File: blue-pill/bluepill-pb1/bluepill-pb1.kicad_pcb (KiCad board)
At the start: 2 copper layers, 102.9 x 68.6 mm, 31 parts, among them J1 pc850vs_11_pin, J2 Conn_01x04, J3 Conn_01x04, J4 Conn_01x04, J5 Conn_01x09, J6 Conn_01x06, J7 Conn_01x02, Q1 Q_NPN_CBE, SW1 Switch_SW_SPST, SW2 Switch_SW_SPST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

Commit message: Added samples
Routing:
- net (no net): vias 107 -> 111
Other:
- board size 102.9 x 68.6 mm -> 102.9 x 88.8 mm
- board text added: "SHARP PC-G850VS Gadget V2.1"
- board text removed: "SHARP PC-G850VS Gadget V2.0"

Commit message: Fix to issue #2
The SD card would sometimes not initialise. A possible fix to this is in this
commit.
By putting a finger on various terminals I found that the CS pin of the SD card adapter
could stop initialisation of the card if it was held high. Holding it low with a high-ish
resistance allowed the SD card to initialise every time. With the theory that the CS line
was activating before or during the SD card initialisation and messing it up, holding it low with a resistor
would deselect it unless the blue pill drove the GPIO high when it wanted ot send a command
or data.
As a test, I have added an explicit GPIO output data direction setup and drive the GPIo to 0 as early
as possible. This does seem to have solved the problem I saw, which hopefully is the problem
seen everywhere.
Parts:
- R1, R16, R17, R2, R3: value R_Small -> 4k7
- R10, R11, R12, R13, R4, R5, R6, R7, R8, R9: value R_Small -> 1k
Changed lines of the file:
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@@
-(kicad_pcb (version 20171130) (host pcbnew 5.1.6-c6e7f7d~86~ubuntu16.04.1)
+(kicad_pcb (version 20171130) (host pcbnew 5.1.5+dfsg1-2build2)
   (general
     (thickness 1.6)
@@
     (add_net "Net-(A1-Pad5)")
     (add_net "Net-(A1-Pad6)")
+    (add_net "Net-(J1-Pad1)")
     (add_net "Net-(J1-Pad10)")
     (add_net "Net-(J1-Pad11)")
@@
     (add_net "Net-(R7-Pad1)")
     (add_net "Net-(R8-Pad1)")
+    (add_net "Net-(U1-PadBOOT)")
+    (add_net "Net-(U1-PadNRST)")
+    (add_net "Net-(U1-PadPB10)")
+    (add_net "Net-(U1-PadPB2)")
+    (add_net "Net-(U1-PadVBAT)")
   )
   (module Connector_PinHeader_2.54mm:PinHeader_1x06_P2.54mm_Vertical (layer F.Cu)
@@
       (effects (font (size 1 1) (thickness 0.15)))
     )
-    (fp_text value R_Small (at 3.81 2.37) (layer F.Fab)
+    (fp_text value 4k7 (at 3.81 2.37) (layer F.Fab)
       (effects (font (size 1 1) (thickness 0.15)))
     )
@@
       (effects (font (size 1 1) (thickness 0.15)))
     )
-    (fp_text value R_Small (at 3.81 2.37 90) (layer F.Fab)
+    (fp_text value 4k7 (at 3.81 2.37 90) (layer F.Fab)
       (effects (font (size 1 1) (thickness 0.15)))
     )
@@
       (effects (font (size 1 1) (thickness 0.15)))
     )
-    (fp_text value R_Small (at 3.81 2.37) (layer F.Fab)
+    (fp_text value 1k (at 3.81 2.37) (layer F.Fab)
       (effects (font (size 1 1) (thickness 0.15)))
     )
@@
       (effects (font (size 1 1) (thickness 0.15)))
     )
-    (fp_text value R_Small (at 3.81 2.37) (layer F.Fab)
+    (fp_text value 1k (at 3.81 2.37) (layer F.Fab)
       (effects (font (size 1 1) (thickness 0.15)))
     )
@@
       (effects (font (size 1 1) (thickness 0.15)))
     )
-    (fp_text value R_Small (at 3.81 2.37) (layer F.Fab)
+    (fp_text value 1k (at 3.81 2.37) (layer F.Fab)
       (effects (font (size 1 1) (thickness 0.15)))
     )
@@
       (effects (font (size 1 1) (thickness 0.15)))
     )
-    (fp_text value R_Small (at 3.81 2.37) (layer F.Fab)
+    (fp_text value 1k (at 3.81 2.37) (layer F.Fab)
       (effects (font (size 1 1) (thickness 0.15)))
     )
@@
       (effects (font (size 1 1) (thickness 0.15)))
     )
-    (fp_text value R_Small (at 3.81 2.37) (layer F.Fab)
+    (fp_text value 1k (at 3.81 2.37) (layer F.Fab)
       (effects (font (size 1 1) (thickness 0.15)))
     )
@@
       (effects (font (size 1 1) (thickness 0.15)))
     )
-    (fp_text value R_Small (at 3.81 2.37) (layer F.Fab)
+    (fp_text value 1k (at 3.81 2.37) (layer F.Fab)
       (effects (font (size 1 1) (thickness 0.15)))
     )
@@
       (effects (font (size 1 1) (thickness 0.15)))
     )
-    (fp_text value R_Small (at 3.81 2.37) (layer F.Fab)
+    (fp_text value 1k (at 3.81 2.37) (layer F.Fab)
       (effects (font (size 1 1) (thickness 0.15)))
     )
@@
       (effects (font (size 1 1) (thickness 0.15)))
     )
-    (fp_text value R_Small (at 3.81 2.37) (layer F.Fab)
+    (fp_text value 1k (at 3.81 2.37) (layer F.Fab)
       (effects (font (size 1 1) (thickness 0.15)))
     )
@@
       (effects (font (size 1 1) (thickness 0.15)))
     )
-    (fp_text value R_Small (at 3.81 2.37) (layer F.Fab)
+    (fp_text value 1k (at 3.81 2.37) (layer F.Fab)
       (effects (font (size 1 1) (thickness 0.15)))
     )
@@
       (effects (font (size 1 1) (thickness 0.15)))
     )
-    (fp_text value R_Small (at 3.81 2.37) (layer F.Fab)
+    (fp_text value 1k (at 3.81 2.37) (layer F.Fab)
       (effects (font (size 1 1) (thickness 0.15)))
     )
@@
       (effects (font (size 1 1) (thickness 0.15)))
     )
-    (fp_text value R_Small (at 3.81 2.37) (layer F.Fab)
+    (fp_text value 4k7 (at 3.81 2.37) (layer F.Fab)
       (effects (font (size 1 1) (thickness 0.15)))
     )
@@
       (effects (font (size 1 1) (thickness 0.15)))
     )
-    (fp_text value R_Small (at 3.81 2.37) (layer F.Fab)
+    (fp_text value 4k7 (at 3.81 2.37) (layer F.Fab)
       (effects (font (size 1 1) (thickness 0.15)))
     )
@@
       (effects (font (size 1 1) (thickness 0.15)))
     )
-    (fp_text value R_Small (at 3.81 2.37) (layer F.Fab)
-      (effects (font (size 1 1) (thickness 0.15)))
-    )
+    (fp_text value 4k7 (at 3.81 2.37) (layer F.Fab)
+      (effects (font (size 1 1) (thickness 0.15)))
+    )

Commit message: Updates
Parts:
- R14, R15: value R_Small -> Do not fit
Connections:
- A1 pad 2: +3V3 -> Net-(A1-Pad2)
- J6 pad 1: Net-(J6-Pad1) -> Net-(A1-Pad2)
- J7 pad 2: Net-(J6-Pad1) -> Net-(A1-Pad2)
- U1 pad 5V: Net-(J6-Pad1) -> Net-(A1-Pad2)
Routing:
- net Net-(A1-Pad2): track 0.00 -> 193.2 mm, vias 0 -> 5
- net Net-(J6-Pad1): track 130.2 -> 0.00 mm, vias 3 -> 0
- net +3V3: track 284.4 -> 280.6 mm

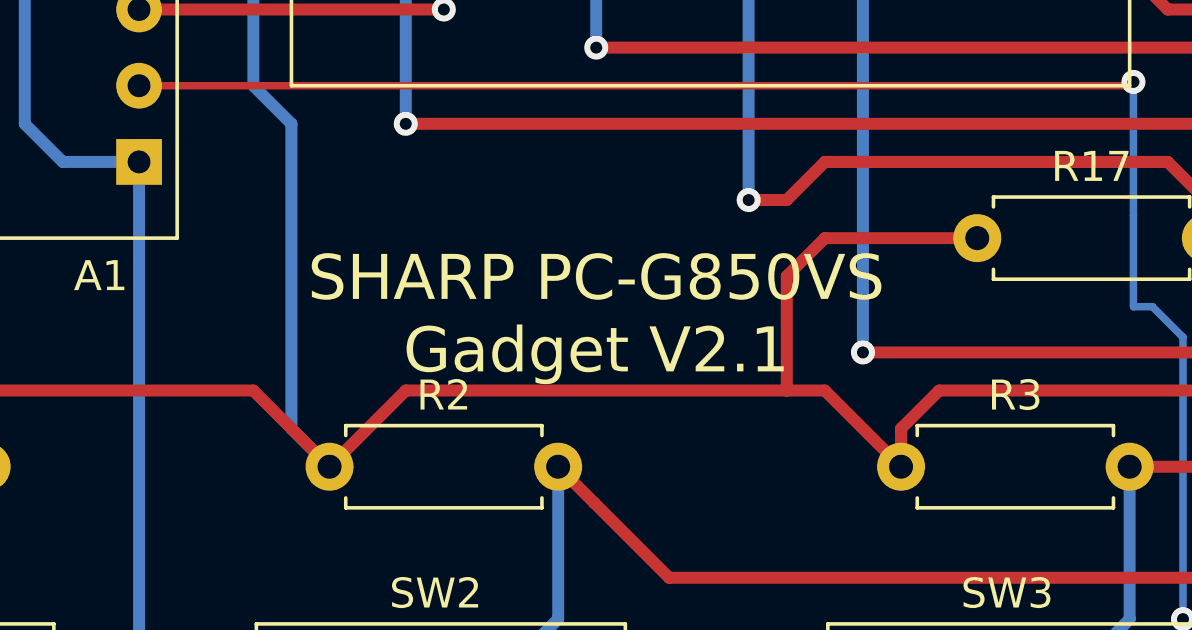
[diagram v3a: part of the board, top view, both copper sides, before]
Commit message: Added PCB V2.2, which fixes the wire needed on V2.1
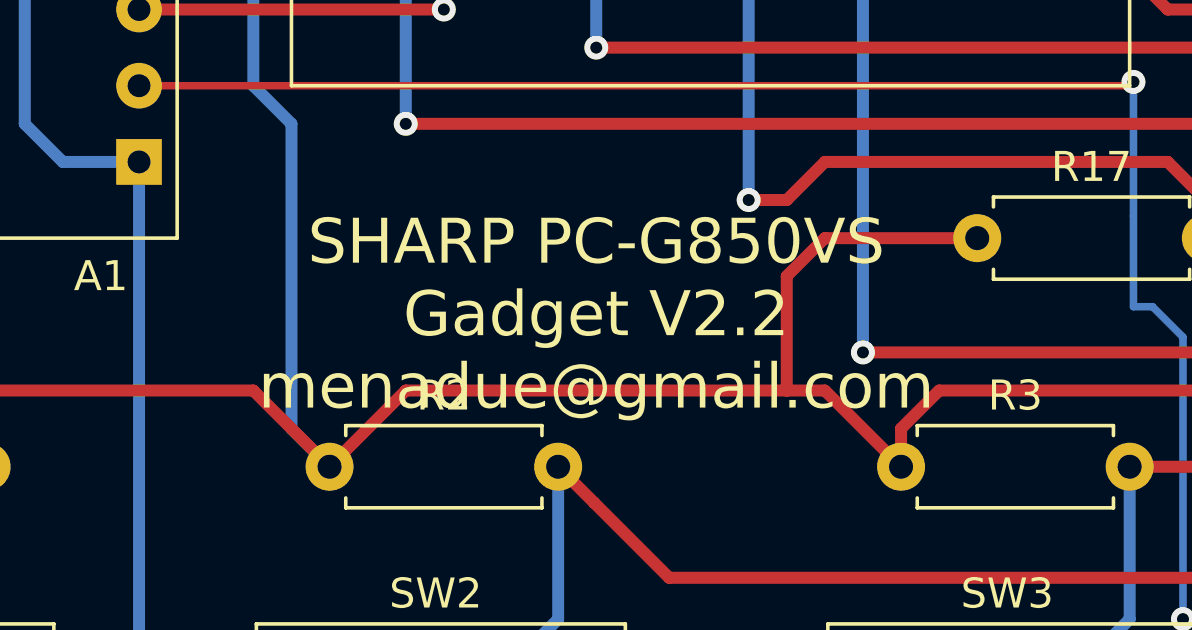
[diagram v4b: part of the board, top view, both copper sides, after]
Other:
- board text added: "SHARP PC-G850VS Gadget V2.2 menadue@gmail.com"
- board text removed: "SHARP PC-G850VS Gadget V2.1"
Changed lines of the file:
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@@
   (gr_line (start 179.07 115.58) (end 179.07 135.8) (layer Edge.Cuts) (width 0.05))
   (gr_line (start 76.2 115.58) (end 76.2 135.8) (layer Edge.Cuts) (width 0.05))
-  (gr_text "SHARP PC-G850VS\nGadget V2.1" (at 110.49 99.06) (layer F.SilkS)
+  (gr_text "SHARP PC-G850VS\nGadget V2.2\nmenadue@gmail.com" (at 110.49 99.06) (layer F.SilkS)
     (effects (font (size 1.5 1.5) (thickness 0.3)))
   )
